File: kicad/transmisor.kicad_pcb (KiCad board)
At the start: 4 copper layers, 48 x 19.9 mm, 46 parts, among them J1 USB_B_Micro, J2 Conn_02x05_Odd_Even, J3 Conn_01x03_Female, J4 Conn_01x04_Female, SW1 SW_Push_Dual, U1 NRF24L01+, U2 CH330N, U3 XC6206PxxxMR, U4 STM32G031F8Px, U5 USBLC6-2SC6, U6 MPU-6050, Y1 16 MHz

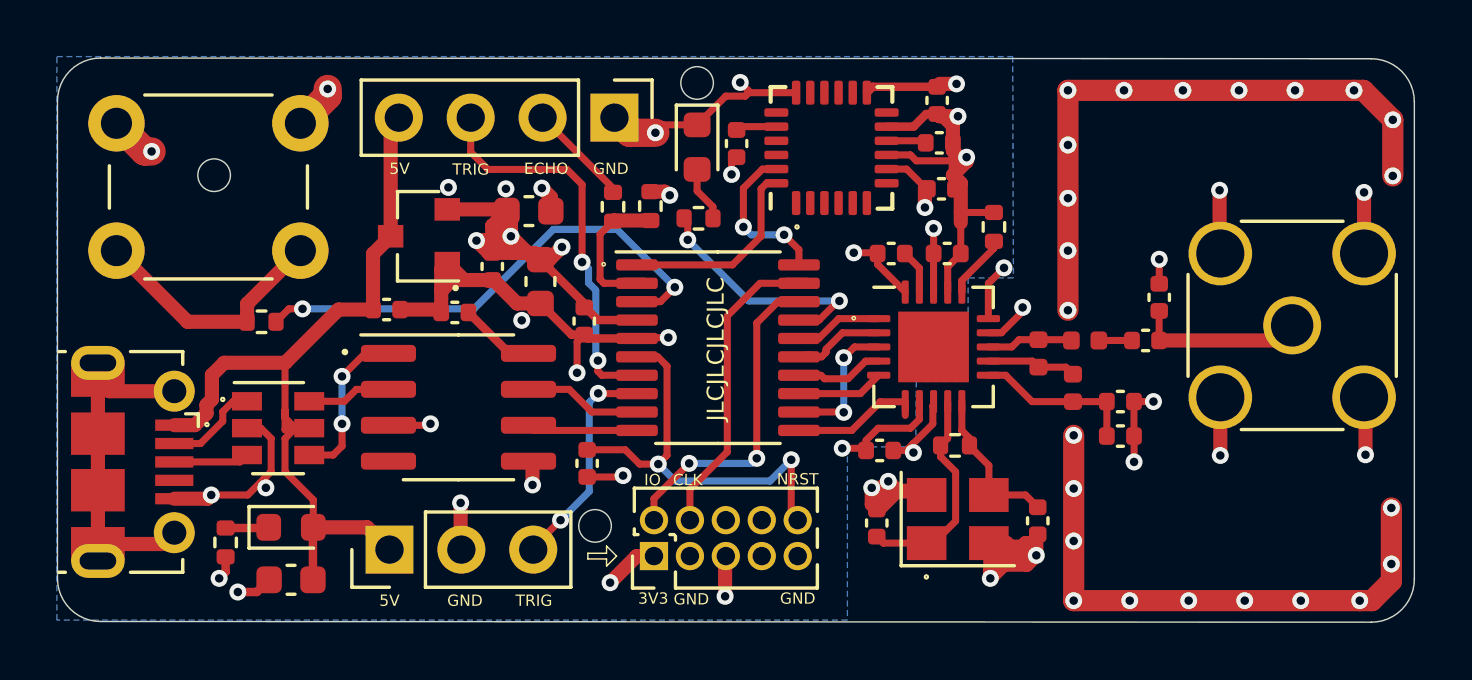
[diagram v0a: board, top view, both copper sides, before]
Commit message: Mejoraste la interfaz PWM. Agregaste la capacidad de habilitar salida de varios canales.
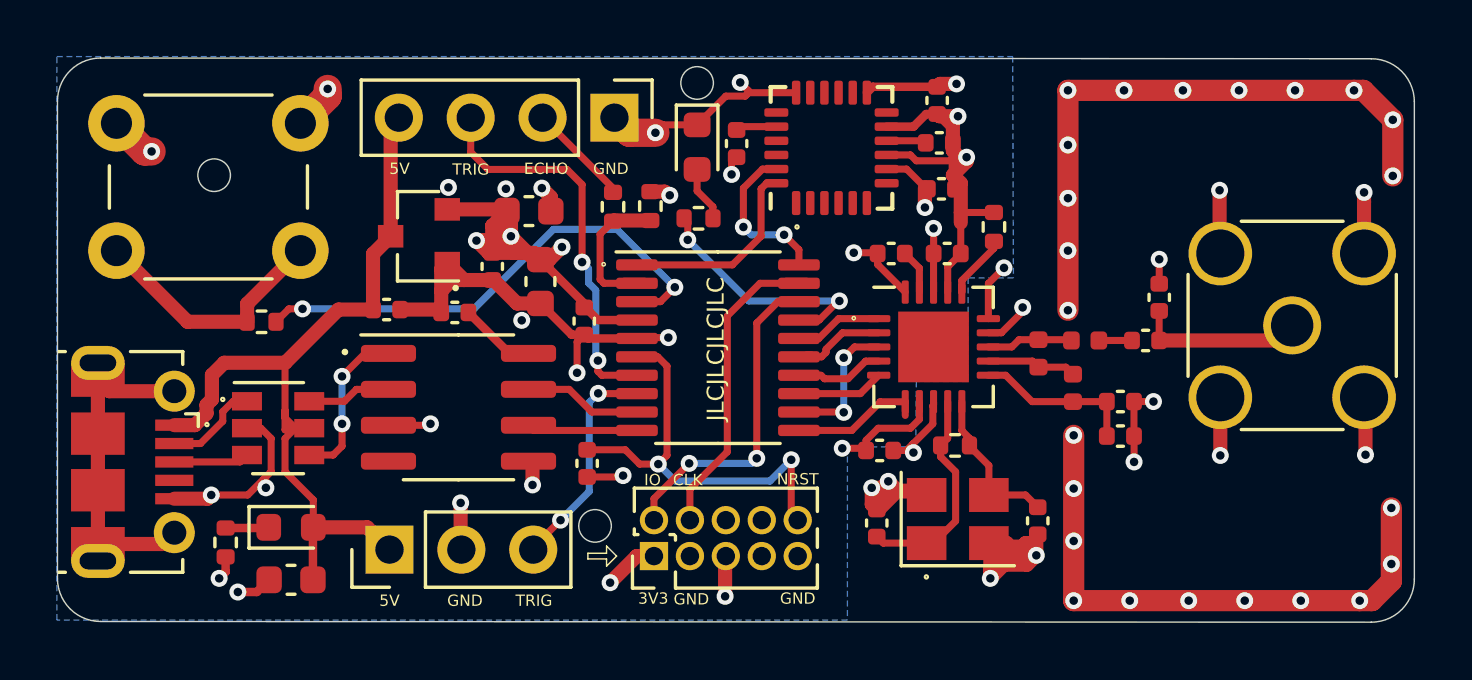
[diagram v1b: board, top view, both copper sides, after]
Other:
- net class Default removed
